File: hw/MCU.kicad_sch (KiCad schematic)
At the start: 13 parts

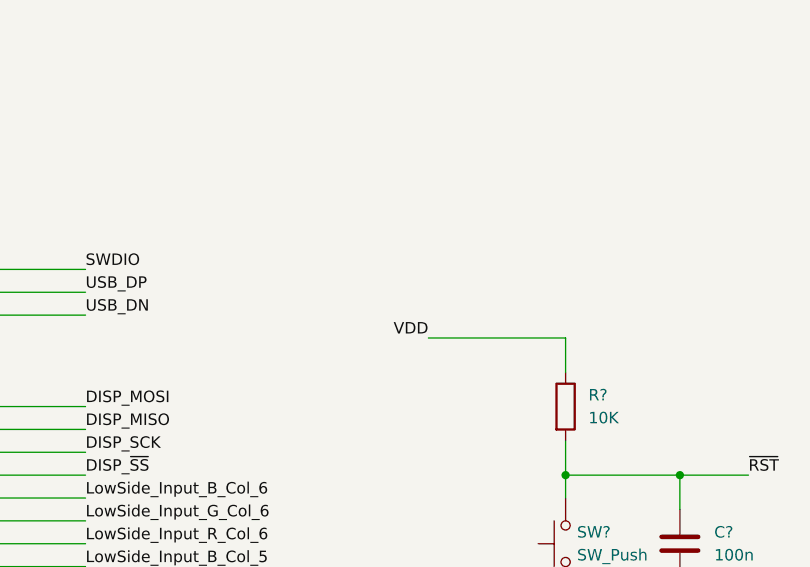
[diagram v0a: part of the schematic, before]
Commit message: USB Type-C Connector
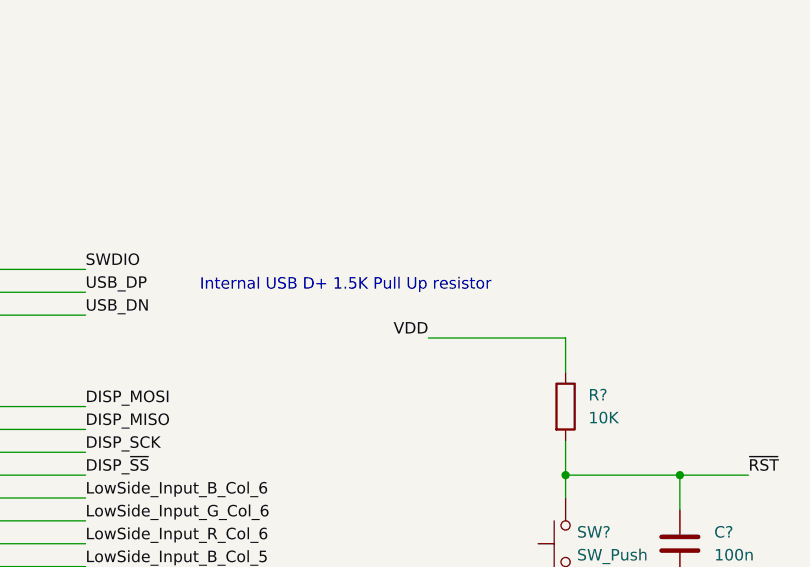
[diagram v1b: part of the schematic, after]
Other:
- note added: "Internal USB D+ 1.5K Pull Up resistor"
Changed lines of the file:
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@@
     )
+  )
+  (text "Internal USB D+ 1.5K Pull Up resistor" (at 213.36 83.82 0)
+    (effects (font (size 1.27 1.27)) (justify left bottom))
   )
   (text "100nF for VRef" (at 198.12 34.29 0)

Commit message: setup components information
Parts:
- C? (x5): LCSC (none) -> C126469; Vendor (none) -> TORCH(火炬); Vendor Model (none) -> CT41G-0805-2X1-50V-0.1μF
- C?: LCSC (none) -> C28323; Vendor (none) -> SAMSUNG(三星); Vendor Model (none) -> CL21B105KBFNNNE
- C?: LCSC (none) -> C1710; Vendor (none) -> SAMSUNG(三星); Vendor Model (none) -> CL21B103KBANNNC
- C?: LCSC (none) -> C1779; Vendor (none) -> SAMSUNG(三星); Vendor Model (none) -> CL21A475KAQNNNE
- R? (x2): LCSC (none) -> C17414; Vendor (none) -> UNI-ROYAL(厚声); Vendor Model (none) -> 0805W8F1002T5E
- U?: LCSC (none) -> C2981445; Vendor (none) -> Nations(国民技术); Vendor Model (none) -> N32L406RBL7
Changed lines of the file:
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@@
       (effects (font (size 1.27 1.27)) hide)
     )
-    (property "Description" "" (at 241.3 26.67 0)
-      (effects (font (size 1.27 1.27)) hide)
-    )
-    (property "LCSC" "" (at 241.3 26.67 0)
-      (effects (font (size 1.27 1.27)) hide)
-    )
-    (property "Vendor" "" (at 241.3 26.67 0)
-      (effects (font (size 1.27 1.27)) hide)
-    )
-    (property "Vendor Model" "" (at 241.3 26.67 0)
+    (property "Description" "容值: 100nF 精度: ±10% 额定电压: 50V 材质(温度系数): 2X1 材质:2X1(X7R)" (at 241.3 26.67 0)
+      (effects (font (size 1.27 1.27)) hide)
+    )
+    (property "LCSC" "C126469" (at 241.3 26.67 0)
+      (effects (font (size 1.27 1.27)) hide)
+    )
+    (property "Vendor" "TORCH(火炬)" (at 241.3 26.67 0)
+      (effects (font (size 1.27 1.27)) hide)
+    )
+    (property "Vendor Model" "CT41G-0805-2X1-50V-0.1μF" (at 241.3 26.67 0)
       (effects (font (size 1.27 1.27)) hide)
     )
@@
       (effects (font (size 1.27 1.27)) hide)
     )
-    (property "Description" "" (at 264.16 149.86 0)
-      (effects (font (size 1.27 1.27)) hide)
-    )
-    (property "LCSC" "" (at 264.16 149.86 0)
-      (effects (font (size 1.27 1.27)) hide)
-    )
-    (property "Vendor" "" (at 264.16 149.86 0)
-      (effects (font (size 1.27 1.27)) hide)
-    )
-    (property "Vendor Model" "" (at 264.16 149.86 0)
+    (property "Description" "电阻类型: 厚膜电阻 阻值: 10kΩ 精度: ±1% 功率: 1/8W 温度系数: ±100ppm/℃ 最大工作电压: 150V 工作温度" (at 264.16 149.86 0)
+      (effects (font (size 1.27 1.27)) hide)
+    )
+    (property "LCSC" "C17414" (at 264.16 149.86 0)
+      (effects (font (size 1.27 1.27)) hide)
+    )
+    (property "Vendor" "UNI-ROYAL(厚声)" (at 264.16 149.86 0)
+      (effects (font (size 1.27 1.27)) hide)
+    )
+    (property "Vendor Model" "0805W8F1002T5E" (at 264.16 149.86 0)
       (effects (font (size 1.27 1.27)) hide)
     )
@@
       (effects (font (size 1.27 1.27)) hide)
     )
-    (property "Description" "" (at 266.7 111.76 0)
-      (effects (font (size 1.27 1.27)) hide)
-    )
-    (property "LCSC" "" (at 266.7 111.76 0)
-      (effects (font (size 1.27 1.27)) hide)
-    )
-    (property "Vendor" "" (at 266.7 111.76 0)
-      (effects (font (size 1.27 1.27)) hide)
-    )
-    (property "Vendor Model" "" (at 266.7 111.76 0)
+    (property "Description" "容值: 100nF 精度: ±10% 额定电压: 50V 材质(温度系数): 2X1 材质:2X1(X7R)" (at 266.7 111.76 0)
+      (effects (font (size 1.27 1.27)) hide)
+    )
+    (property "LCSC" "C126469" (at 266.7 111.76 0)
+      (effects (font (size 1.27 1.27)) hide)
+    )
+    (property "Vendor" "TORCH(火炬)" (at 266.7 111.76 0)
+      (effects (font (size 1.27 1.27)) hide)
+    )
+    (property "Vendor Model" "CT41G-0805-2X1-50V-0.1μF" (at 266.7 111.76 0)
       (effects (font (size 1.27 1.27)) hide)
     )
@@
       (effects (font (size 1.27 1.27)) hide)
     )
-    (property "Description" "" (at 181.61 26.67 0)
-      (effects (font (size 1.27 1.27)) hide)
-    )
-    (property "LCSC" "" (at 181.61 26.67 0)
-      (effects (font (size 1.27 1.27)) hide)
-    )
-    (property "Vendor" "" (at 181.61 26.67 0)
-      (effects (font (size 1.27 1.27)) hide)
-    )
-    (property "Vendor Model" "" (at 181.61 26.67 0)
+    (property "Description" "容值: 1uF 精度: ±10% 额定电压: 50V 材质(温度系数): X7R 材质:X7R" (at 181.61 26.67 0)
+      (effects (font (size 1.27 1.27)) hide)
+    )
+    (property "LCSC" "C28323" (at 181.61 26.67 0)
+      (effects (font (size 1.27 1.27)) hide)
+    )
+    (property "Vendor" "SAMSUNG(三星)" (at 181.61 26.67 0)
+      (effects (font (size 1.27 1.27)) hide)
+    )
+    (property "Vendor Model" "CL21B105KBFNNNE" (at 181.61 26.67 0)
       (effects (font (size 1.27 1.27)) hide)
     )
@@
       (effects (font (size 1.27 1.27)) hide)
     )
-    (property "Description" "" (at 227.33 26.67 0)
-      (effects (font (size 1.27 1.27)) hide)
-    )
-    (property "LCSC" "" (at 227.33 26.67 0)
-      (effects (font (size 1.27 1.27)) hide)
-    )
-    (property "Vendor" "" (at 227.33 26.67 0)
-      (effects (font (size 1.27 1.27)) hide)
-    )
-    (property "Vendor Model" "" (at 227.33 26.67 0)
+    (property "Description" "容值: 100nF 精度: ±10% 额定电压: 50V 材质(温度系数): 2X1 材质:2X1(X7R)" (at 227.33 26.67 0)
+      (effects (font (size 1.27 1.27)) hide)
+    )
+    (property "LCSC" "C126469" (at 227.33 26.67 0)
+      (effects (font (size 1.27 1.27)) hide)
+    )
+    (property "Vendor" "TORCH(火炬)" (at 227.33 26.67 0)
+      (effects (font (size 1.27 1.27)) hide)
+    )
+    (property "Vendor Model" "CT41G-0805-2X1-50V-0.1μF" (at 227.33 26.67 0)
       (effects (font (size 1.27 1.27)) hide)
     )
@@
       (effects (font (size 1.27 1.27)) hide)
     )
-    (property "Description" "" (at 254 96.52 0)
-      (effects (font (size 1.27 1.27)) hide)
-    )
-    (property "LCSC" "" (at 254 96.52 0)
-      (effects (font (size 1.27 1.27)) hide)
-    )
-    (property "Vendor" "" (at 254 96.52 0)
-      (effects (font (size 1.27 1.27)) hide)
-    )
-    (property "Vendor Model" "" (at 254 96.52 0)
+    (property "Description" "电阻类型: 厚膜电阻 阻值: 10kΩ 精度: ±1% 功率: 1/8W 温度系数: ±100ppm/℃ 最大工作电压: 150V 工作温度" (at 254 96.52 0)
+      (effects (font (size 1.27 1.27)) hide)
+    )
+    (property "LCSC" "C17414" (at 254 96.52 0)
+      (effects (font (size 1.27 1.27)) hide)
+    )
+    (property "Vendor" "UNI-ROYAL(厚声)" (at 254 96.52 0)
+      (effects (font (size 1.27 1.27)) hide)
+    )
+    (property "Vendor Model" "0805W8F1002T5E" (at 254 96.52 0)
       (effects (font (size 1.27 1.27)) hide)
     )
@@
       (effects (font (size 1.27 1.27)) hide)
     )
-    (property "Description" "" (at 193.04 26.67 0)
-      (effects (font (size 1.27 1.27)) hide)
-    )
-    (property "LCSC" "" (at 193.04 26.67 0)
-      (effects (font (size 1.27 1.27)) hide)
-    )
-    (property "Vendor" "" (at 193.04 26.67 0)
-      (effects (font (size 1.27 1.27)) hide)
-    )
-    (property "Vendor Model" "" (at 193.04 26.67 0)
+    (property "Description" "容值: 100nF 精度: ±10% 额定电压: 50V 材质(温度系数): 2X1 材质:2X1(X7R)" (at 193.04 26.67 0)
+      (effects (font (size 1.27 1.27)) hide)
+    )
+    (property "LCSC" "C126469" (at 193.04 26.67 0)
+      (effects (font (size 1.27 1.27)) hide)
+    )
+    (property "Vendor" "TORCH(火炬)" (at 193.04 26.67 0)
+      (effects (font (size 1.27 1.27)) hide)
+    )
+    (property "Vendor Model" "CT41G-0805-2X1-50V-0.1μF" (at 193.04 26.67 0)
       (effects (font (size 1.27 1.27)) hide)
     )
@@
       (effects (font (size 1.27 1.27)) hide)
     )
-    (property "LCSC" "" (at 157.48 99.06 0)
-      (effects (font (size 1.27 1.27)) hide)
-    )
-    (property "Vendor" "" (at 157.48 99.06 0)
-      (effects (font (size 1.27 1.27)) hide)
-    )
-    (property "Vendor Model" "" (at 157.48 99.06 0)
+    (property "LCSC" "C2981445" (at 157.48 99.06 0)
+      (effects (font (size 1.27 1.27)) hide)
+    )
+    (property "Vendor" "Nations(国民技术)" (at 157.48 99.06 0)
+      (effects (font (size 1.27 1.27)) hide)
+    )
+    (property "Vendor Model" "N32L406RBL7" (at 157.48 99.06 0)
       (effects (font (size 1.27 1.27)) hide)
     )
@@
       (effects (font (size 1.27 1.27)) hide)
     )
-    (property "Description" "" (at 254 26.67 0)
-      (effects (font (size 1.27 1.27)) hide)
-    )
-    (property "LCSC" "" (at 254 26.67 0)
-      (effects (font (size 1.27 1.27)) hide)
-    )
-    (property "Vendor" "" (at 254 26.67 0)
-      (effects (font (size 1.27 1.27)) hide)
-    )
-    (property "Vendor Model" "" (at 254 26.67 0)
+    (property "Description" "容值: 100nF 精度: ±10% 额定电压: 50V 材质(温度系数): 2X1 材质:2X1(X7R)" (at 254 26.67 0)
+      (effects (font (size 1.27 1.27)) hide)
+    )
+    (property "LCSC" "C126469" (at 254 26.67 0)
+      (effects (font (size 1.27 1.27)) hide)
+    )
+    (property "Vendor" "TORCH(火炬)" (at 254 26.67 0)
+      (effects (font (size 1.27 1.27)) hide)
+    )
+    (property "Vendor Model" "CT41G-0805-2X1-50V-0.1μF" (at 254 26.67 0)
       (effects (font (size 1.27 1.27)) hide)
     )
@@
       (effects (font (size 1.27 1.27)) hide)
     )
-    (property "Description" "" (at 168.91 26.67 0)
-      (effects (font (size 1.27 1.27)) hide)
-    )
-    (property "LCSC" "" (at 168.91 26.67 0)
-      (effects (font (size 1.27 1.27)) hide)
-    )
-    (property "Vendor" "" (at 168.91 26.67 0)
-      (effects (font (size 1.27 1.27)) hide)
-    )
-    (property "Vendor Model" "" (at 168.91 26.67 0)
+    (property "Description" "容值: 10nF 精度: ±10% 额定电压: 50V 材质(温度系数): X7R 材质:X7R" (at 168.91 26.67 0)
+      (effects (font (size 1.27 1.27)) hide)
+    )
+    (property "LCSC" "C1710" (at 168.91 26.67 0)
+      (effects (font (size 1.27 1.27)) hide)
+    )
+    (property "Vendor" "SAMSUNG(三星)" (at 168.91 26.67 0)
+      (effects (font (size 1.27 1.27)) hide)
+    )
+    (property "Vendor Model" "CL21B103KBANNNC" (at 168.91 26.67 0)
       (effects (font (size 1.27 1.27)) hide)
     )
@@
       (effects (font (size 1.27 1.27)) hide)
     )
-    (property "Description" "" (at 266.7 26.67 0)
-      (effects (font (size 1.27 1.27)) hide)
-    )
-    (property "LCSC" "" (at 266.7 26.67 0)
-      (effects (font (size 1.27 1.27)) hide)
-    )
-    (property "Vendor" "" (at 266.7 26.67 0)
-      (effects (font (size 1.27 1.27)) hide)
-    )
-    (property "Vendor Model" "" (at 266.7 26.67 0)
-      (effects (font (size 1.27 1.27)) hide)
-    )
+    (property "Description" "容值: 4.7uF 精度: ±10% 额定电压: 25V 材质(温度系数): X5R 材质:X5R" (at 266.7 26.67 0)
+      (effects (font (size 1.27 1.27)) hide)
+    )
+    (property "LCSC" "C1779" (at 266.7 26.67 0)
+      (effects (font (size 1.27 1.27)) hide)
+    )
+    (property "Vendor" "SAMSUNG(三星)" (at 266.7 26.67 0)
+      (effects (font (size 1.27 1.27)) hide)
+    )
+    (property "Vendor Model" "CL21A475KAQNNNE" (at 266.7 26.67 0)
+      (effects (font (size 1.27 1.27)) hide)
+    )

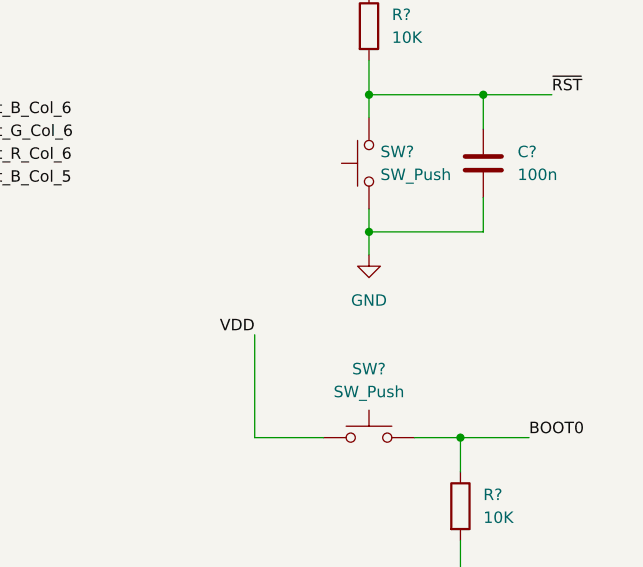
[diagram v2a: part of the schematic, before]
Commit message: added switches
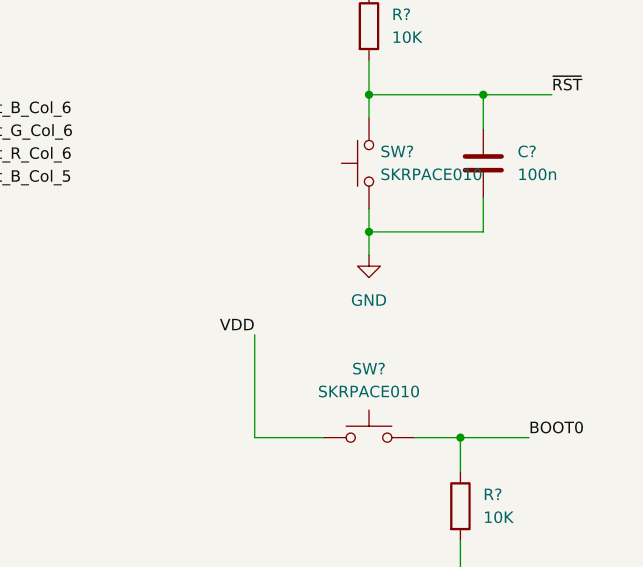
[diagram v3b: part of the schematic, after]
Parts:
- SW? (x2): value SW_Push -> SKRPACE010; footprint (none) -> IotPi_Switch:SKRPACE010
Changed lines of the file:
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@@
       (effects (font (size 1.27 1.27)))
     )
-    (property "Value" "SW_Push" (at 254 137.16 0)
+    (property "Value" "SKRPACE010" (at 254 137.16 0)
       (effects (font (size 1.27 1.27)))
     )
-    (property "Footprint" "" (at 254 137.16 0)
+    (property "Footprint" "IotPi_Switch:SKRPACE010" (at 254 137.16 0)
       (effects (font (size 1.27 1.27)) hide)
     )
@@
       (effects (font (size 1.27 1.27)) (justify right))
     )
-    (property "Value" "SW_Push" (at 255.27 113.03 90)
+    (property "Value" "SKRPACE010" (at 255.27 113.03 90)
       (effects (font (size 1.27 1.27)) (justify right))
     )
-    (property "Footprint" "" (at 248.92 111.76 0)
+    (property "Footprint" "IotPi_Switch:SKRPACE010" (at 248.92 111.76 0)
       (effects (font (size 1.27 1.27)) hide)
     )
@@
   (symbol (lib_id "power:GND") (at 114.3 177.8 0) (unit 1)
     (in_bom yes) (on_board yes) (dnp no) (fields_autoplaced)
-    (property "Reference" "#PWR0202" (at 114.3 184.15 0)
+    (property "Reference" "#PWR?" (at 114.3 184.15 0)
       (effects (font (size 1.27 1.27)) hide)
     )
@@
       (project "KiConSZ2023"
         (path "/8659c260-f029-4e72-8b9a-85fff45eea40/aebeadc6-0cb2-44f8-88a5-80ae76b1b2bc"
-          (reference "#PWR0202") (unit 1)
+          (reference "#PWR?") (unit 1)
         )
       )
@@
   (symbol (lib_id "power:GND") (at 264.16 157.48 0) (unit 1)
     (in_bom yes) (on_board yes) (dnp no) (fields_autoplaced)
-    (property "Reference" "#PWR0204" (at 264.16 163.83 0)
+    (property "Reference" "#PWR?" (at 264.16 163.83 0)
       (effects (font (size 1.27 1.27)) hide)
     )
@@
       (project "KiConSZ2023"
         (path "/8659c260-f029-4e72-8b9a-85fff45eea40/aebeadc6-0cb2-44f8-88a5-80ae76b1b2bc"
-          (reference "#PWR0204") (unit 1)
+          (reference "#PWR?") (unit 1)
         )
       )
@@
   (symbol (lib_id "power:GND") (at 254 121.92 0) (unit 1)
     (in_bom yes) (on_board yes) (dnp no) (fields_autoplaced)
-    (property "Reference" "#PWR0203" (at 254 128.27 0)
+    (property "Reference" "#PWR?" (at 254 128.27 0)
       (effects (font (size 1.27 1.27)) hide)
     )
@@
       (project "KiConSZ2023"
         (path "/8659c260-f029-4e72-8b9a-85fff45eea40/aebeadc6-0cb2-44f8-88a5-80ae76b1b2bc"
-          (reference "#PWR0203") (unit 1)
+          (reference "#PWR?") (unit 1)
         )
       )
@@
   (symbol (lib_id "power:VDD") (at 40.64 26.67 0) (unit 1)
     (in_bom yes) (on_board yes) (dnp no)
-    (property "Reference" "#PWR0201" (at 40.64 30.48 0)
+    (property "Reference" "#PWR?" (at 40.64 30.48 0)
       (effects (font (size 1.27 1.27)) hide)
     )
@@
       (project "KiConSZ2023"
         (path "/8659c260-f029-4e72-8b9a-85fff45eea40/aebeadc6-0cb2-44f8-88a5-80ae76b1b2bc"
-          (reference "#PWR0201") (unit 1)
+          (reference "#PWR?") (unit 1)
         )
       )
